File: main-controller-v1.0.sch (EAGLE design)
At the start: 28 parts, among them IC21 TCA9539PW, J1 PJ-3200-STEREO-JACK, M1 TEENSY4.1-BARE

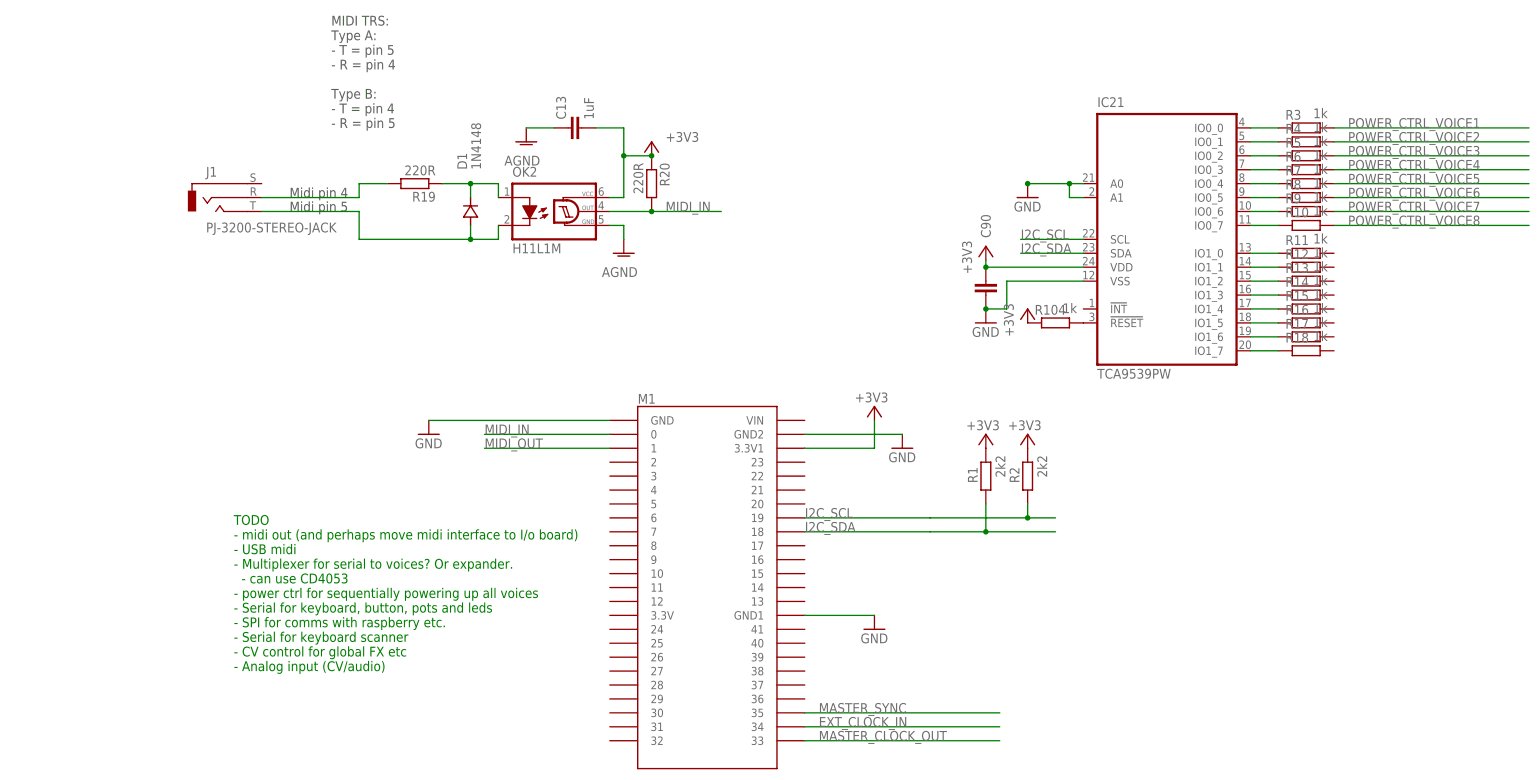
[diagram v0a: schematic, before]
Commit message: Added voice sensing
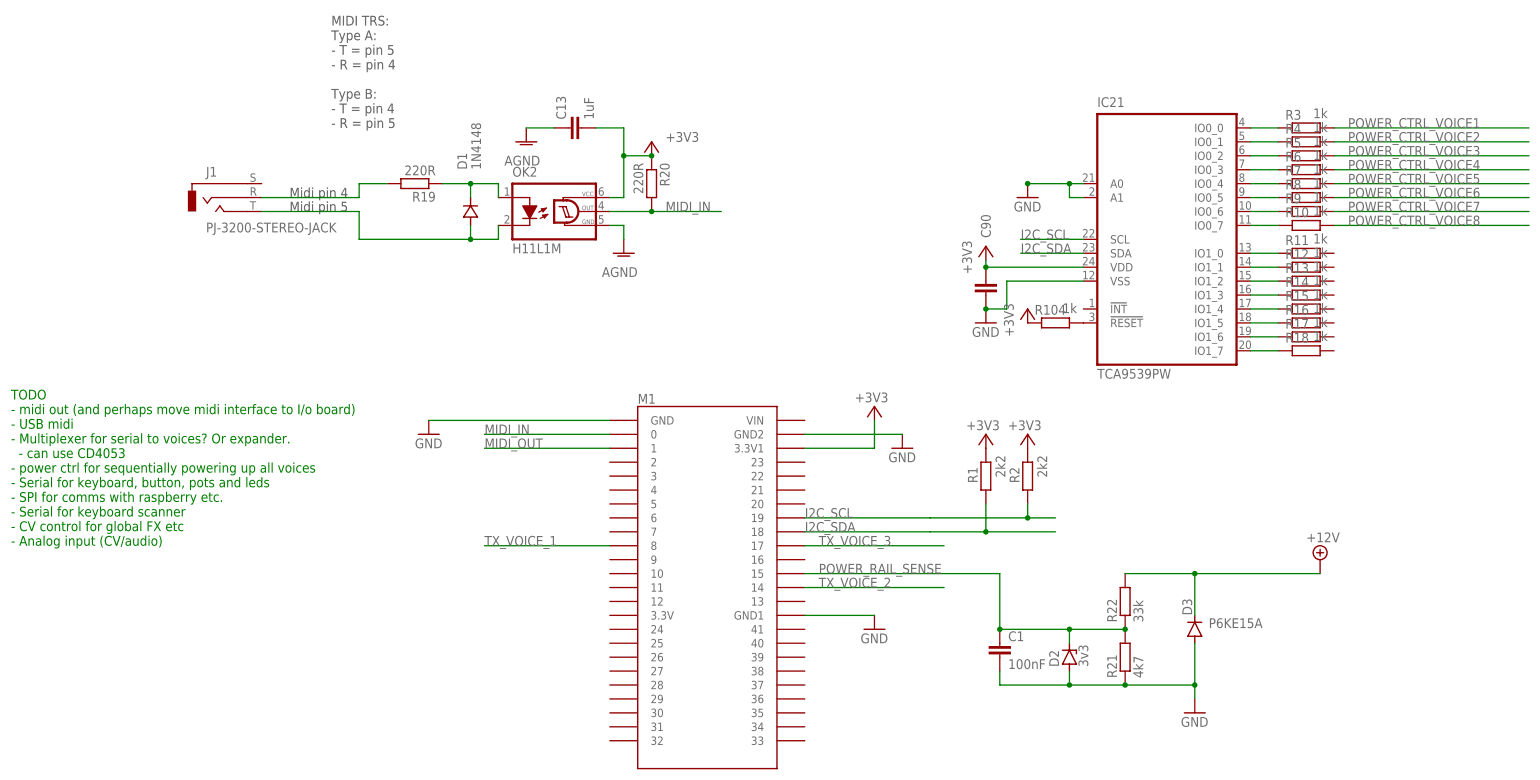
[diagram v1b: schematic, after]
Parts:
- added C1: 100nF, rcl:C-EUC0603
- added D2: 3v3, diode:ZENER-DIODEZD-5
- added D3: P6KE15A, diode:DIODE-D-10
- added R21: 4k7, rcl:R-EU_R0603
- added R22: 33k, rcl:R-EU_R0603
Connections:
- removed net EXT_CLOCK_IN: M1.34
- removed net MASTER_CLOCK_OUT: M1.33
- removed net MASTER_SYNC: M1.35
- new net +12V: D3.C, R22.2
- new net POWER_RAIL_SENSE: C1.1, D2.C, M1.15, R21.2, R22.1
- new net TX_VOICE_1: M1.8
- new net TX_VOICE_2: M1.14
- new net TX_VOICE_3: M1.17
- net GND: now also C1.2, D2.A, D3.A, R21.1
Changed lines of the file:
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@@
 <setting verticaltext="up"/>
 </settings>
-<grid distance="0.1" unitdist="inch" unit="inch" style="dots" multiple="1" display="yes" altdistance="0.01" altunitdist="inch" altunit="inch"/>
+<grid distance="0.1" unitdist="inch" unit="inch" style="lines" multiple="1" display="no" altdistance="0.01" altunitdist="inch" altunit="inch"/>
 <layers>
 <layer number="1" name="Top" color="4" fill="1" visible="no" active="no"/>
@@
 <part name="AGND36" library="supply1" library_urn="urn:adsk.eagle:library:371" deviceset="AGND" device=""/>
 <part name="J1" library="joakim" deviceset="PJ-3200-STEREO-JACK" device=""/>
+<part name="D2" library="diode" library_urn="urn:adsk.eagle:library:210" deviceset="ZENER-DIODE" device="ZD-5" package3d_urn="urn:adsk.eagle:package:43412/1" value="3v3"/>
+<part name="C1" library="rcl" library_urn="urn:adsk.eagle:library:334" deviceset="C-EU" device="C0603" package3d_urn="urn:adsk.eagle:package:23616/2" value="100nF"/>
+<part name="R21" library="rcl" library_urn="urn:adsk.eagle:library:334" deviceset="R-EU_" device="R0603" package3d_urn="urn:adsk.eagle:package:23555/3" value="4k7"/>
+<part name="R22" library="rcl" library_urn="urn:adsk.eagle:library:334" deviceset="R-EU_" device="R0603" package3d_urn="urn:adsk.eagle:package:23555/3" value="33k"/>
+<part name="SUPPLY1" library="supply2" library_urn="urn:adsk.eagle:library:372" deviceset="+12V" device=""/>
+<part name="D3" library="diode" library_urn="urn:adsk.eagle:library:210" deviceset="DIODE-" device="D-10" package3d_urn="urn:adsk.eagle:package:43434/1" value="P6KE15A"/>
+<part name="GND6" library="supply1" library_urn="urn:adsk.eagle:library:371" deviceset="GND" device=""/>
 </parts>
 <sheets>
@@
 - T = pin 4
 - R = pin 5</text>
-<text x="-10.16" y="-17.78" size="1.778" layer="91">TODO
+<text x="-50.8" y="5.08" size="1.778" layer="91">TODO
 - midi out (and perhaps move midi interface to I/o board)
 - USB midi
@@
 <attribute name="VALUE" x="-15.24" y="62.23" size="1.778" layer="96"/>
 </instance>
+<instance part="D2" gate="G$1" x="142.24" y="-15.24" smashed="yes" rot="R90">
+<attribute name="NAME" x="140.335" y="-17.018" size="1.778" layer="95" rot="R90"/>
+<attribute name="VALUE" x="145.669" y="-17.018" size="1.778" layer="96" rot="R90"/>
+</instance>
+<instance part="C1" gate="G$1" x="129.54" y="-12.7" smashed="yes">
+<attribute name="NAME" x="131.064" y="-12.319" size="1.778" layer="95"/>
+<attribute name="VALUE" x="131.064" y="-17.399" size="1.778" layer="96"/>
+</instance>
+<instance part="R21" gate="G$1" x="152.4" y="-15.24" smashed="yes" rot="R90">
+<attribute name="NAME" x="150.9014" y="-19.05" size="1.778" layer="95" rot="R90"/>
+<attribute name="VALUE" x="155.702" y="-19.05" size="1.778" layer="96" rot="R90"/>
+</instance>
+<instance part="R22" gate="G$1" x="152.4" y="-5.08" smashed="yes" rot="R90">
+<attribute name="NAME" x="150.9014" y="-8.89" size="1.778" layer="95" rot="R90"/>
+<attribute name="VALUE" x="155.702" y="-8.89" size="1.778" layer="96" rot="R90"/>
+</instance>
+<instance part="SUPPLY1" gate="+12V" x="187.96" y="2.54" smashed="yes">
+<attribute name="VALUE" x="185.42" y="5.715" size="1.778" layer="96"/>
+</instance>
+<instance part="D3" gate="G$1" x="165.1" y="-10.16" smashed="yes" rot="R90">
+<attribute name="NAME" x="164.6174" y="-7.62" size="1.778" layer="95" rot="R90"/>
+<attribute name="VALUE" x="167.64" y="-9.9314" size="1.778" layer="96"/>
+</instance>
+<instance part="GND6" gate="1" x="165.1" y="-25.4" smashed="yes">
+<attribute name="VALUE" x="162.56" y="-27.94" size="1.778" layer="96"/>
+</instance>
 </instances>
 <busses>
@@
 <wire x1="111.76" y1="25.4" x2="93.98" y2="25.4" width="0.1524" layer="91"/>
 </segment>
+<segment>
+<pinref part="C1" gate="G$1" pin="2"/>
+<wire x1="129.54" y1="-17.78" x2="129.54" y2="-20.32" width="0.1524" layer="91"/>
+<pinref part="R21" gate="G$1" pin="1"/>
+<wire x1="129.54" y1="-20.32" x2="142.24" y2="-20.32" width="0.1524" layer="91"/>
+<pinref part="D2" gate="G$1" pin="A"/>
+<wire x1="142.24" y1="-20.32" x2="152.4" y2="-20.32" width="0.1524" layer="91"/>
+<wire x1="142.24" y1="-17.78" x2="142.24" y2="-20.32" width="0.1524" layer="91"/>
+<junction x="142.24" y="-20.32"/>
+<pinref part="D3" gate="G$1" pin="A"/>
+<wire x1="165.1" y1="-12.7" x2="165.1" y2="-20.32" width="0.1524" layer="91"/>
+<wire x1="165.1" y1="-20.32" x2="165.1" y2="-22.86" width="0.1524" layer="91"/>
+<wire x1="152.4" y1="-20.32" x2="165.1" y2="-20.32" width="0.1524" layer="91"/>
+<junction x="152.4" y="-20.32"/>
+<junction x="165.1" y="-20.32"/>
+<pinref part="GND6" gate="1" pin="GND"/>
+</segment>
 </net>
 <net name="AGND" class="0">
@@
 </segment>
 </net>
-<net name="MASTER_CLOCK_OUT" class="0">
-<segment>
-<pinref part="M1" gate="G$1" pin="33"/>
-<wire x1="93.98" y1="-30.48" x2="129.54" y2="-30.48" width="0.1524" layer="91"/>
-<label x="96.52" y="-30.48" size="1.778" layer="95"/>
-</segment>
-</net>
-<net name="EXT_CLOCK_IN" class="0">
-<segment>
-<pinref part="M1" gate="G$1" pin="34"/>
-<wire x1="93.98" y1="-27.94" x2="129.54" y2="-27.94" width="0.1524" layer="91"/>
-<label x="96.52" y="-27.94" size="1.778" layer="95"/>
-</segment>
-</net>
-<net name="MASTER_SYNC" class="0">
-<segment>
-<pinref part="M1" gate="G$1" pin="35"/>
-<wire x1="93.98" y1="-25.4" x2="129.54" y2="-25.4" width="0.1524" layer="91"/>
-<label x="96.52" y="-25.4" size="1.778" layer="95"/>
+<net name="POWER_RAIL_SENSE" class="0">
+<segment>
+<pinref part="M1" gate="G$1" pin="15"/>
+<wire x1="93.98" y1="0" x2="129.54" y2="0" width="0.1524" layer="91"/>
+<wire x1="129.54" y1="0" x2="129.54" y2="-10.16" width="0.1524" layer="91"/>
+<pinref part="C1" gate="G$1" pin="1"/>
+<junction x="129.54" y="-10.16"/>
+<pinref part="R21" gate="G$1" pin="2"/>
+<pinref part="R22" gate="G$1" pin="1"/>
+<wire x1="129.54" y1="-10.16" x2="142.24" y2="-10.16" width="0.1524" layer="91"/>
+<junction x="152.4" y="-10.16"/>
+<pinref part="D2" gate="G$1" pin="C"/>
+<wire x1="142.24" y1="-10.16" x2="152.4" y2="-10.16" width="0.1524" layer="91"/>
+<wire x1="142.24" y1="-12.7" x2="142.24" y2="-10.16" width="0.1524" layer="91"/>
+<junction x="142.24" y="-10.16"/>
+<label x="96.52" y="0" size="1.778" layer="95"/>
+</segment>
+</net>
+<net name="+12V" class="0">
+<segment>
+<pinref part="R22" gate="G$1" pin="2"/>
+<wire x1="152.4" y1="0" x2="165.1" y2="0" width="0.1524" layer="91"/>
+<pinref part="SUPPLY1" gate="+12V" pin="+12V"/>
+<pinref part="D3" gate="G$1" pin="C"/>
+<wire x1="165.1" y1="0" x2="187.96" y2="0" width="0.1524" layer="91"/>
+<wire x1="165.1" y1="-7.62" x2="165.1" y2="0" width="0.1524" layer="91"/>
+<junction x="165.1" y="0"/>
+</segment>
+</net>
+<net name="TX_VOICE_1" class="0">
+<segment>
+<pinref part="M1" gate="G$1" pin="8"/>
+<wire x1="58.42" y1="5.08" x2="35.56" y2="5.08" width="0.1524" layer="91"/>
+<label x="35.56" y="5.08" size="1.778" layer="95"/>
+</segment>
+</net>
+<net name="TX_VOICE_2" class="0">
+<segment>
+<pinref part="M1" gate="G$1" pin="14"/>
+<wire x1="93.98" y1="-2.54" x2="119.38" y2="-2.54" width="0.1524" layer="91"/>
+<label x="96.52" y="-2.54" size="1.778" layer="95"/>
+</segment>
+</net>
+<net name="TX_VOICE_3" class="0">
+<segment>
+<pinref part="M1" gate="G$1" pin="17"/>
+<wire x1="93.98" y1="5.08" x2="119.38" y2="5.08" width="0.1524" layer="91"/>
+<label x="96.52" y="5.08" size="1.778" layer="95"/>
 </segment>
 </net>
@@
 packages will not be understood (or retained) with this version.
 </note>
+<note version="8.4" severity="warning">
+Since Version 8.4, EAGLE supports properties for SPICE simulation.
+Probes in schematics and SPICE mapping objects found in parts and library devices
+will not be understood with this version. Update EAGLE to the latest version
+for full support of SPICE simulation.
+</note>
 </compatibility>
